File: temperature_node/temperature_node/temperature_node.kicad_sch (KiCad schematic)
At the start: 35 parts, among them CN1 UART, J1 USB_C_Receptacle_USB2.0_16P, J2 S2B-PH-K-S, U1 SHT40-AD1B-R3, U2 MCP73831-2-OT, U3 MIC5504-3.3YM5, U4 ESP32-C3-WROOM-02, U6 USBLC6-2P6

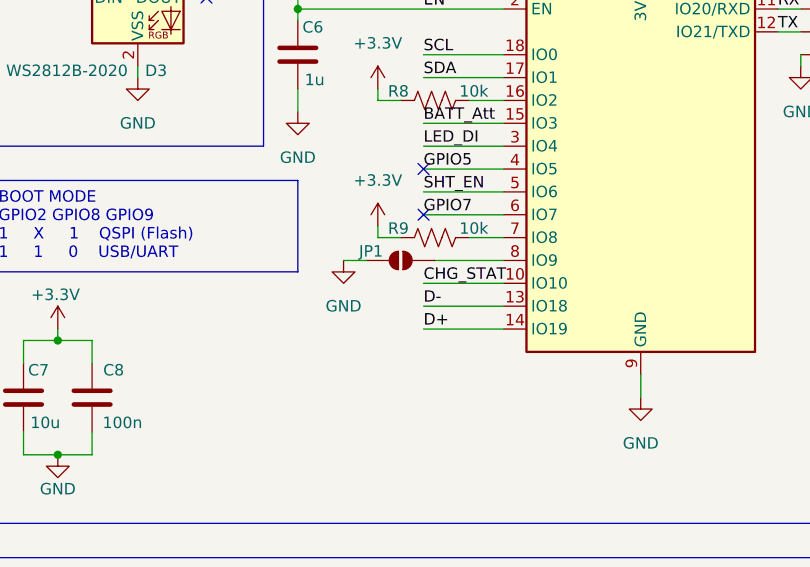
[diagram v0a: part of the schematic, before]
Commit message: Replace pad with side connector for programming enable
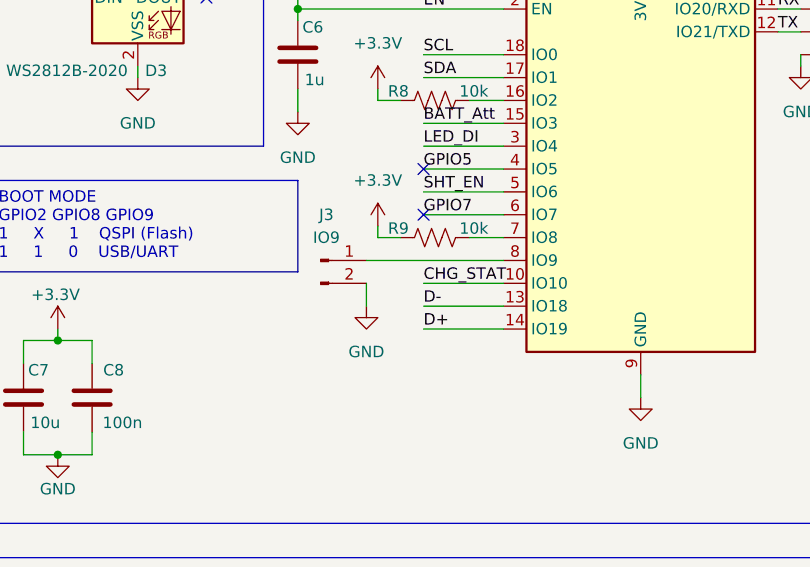
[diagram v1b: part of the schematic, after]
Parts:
- removed JP1: ~, Jumper:SolderJumper-2_P1.3mm_Open_RoundedPad1.0x1.5mm, symbol Jumper:SolderJumper_2_Open
- added J3: IO9, Connector_Wire:SolderWire-0.1sqmm_1x02_P3.6mm_D0.4mm_OD1mm, symbol Connector:Conn_01x02_Pin
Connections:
- net GND: now also J3.2 (Pin_2)
- net at U4.8 (IO9): now also J3.1 (Pin_1)
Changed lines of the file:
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@@
 	(wire
 		(pts
-			(xy 199.39 78.74) (xy 196.85 78.74)
-		)
-		(stroke
-			(width 0)
-			(type default)
-		)
-	)
-	(wire
-		(pts
 			(xy 63.5 52.07) (xy 77.47 52.07)
 		)
@@
 	(wire
 		(pts
+			(xy 199.39 78.74) (xy 214.63 78.74)
+		)
+		(stroke
+			(width 0)
+			(type default)
+		)
+	)
+	(wire
+		(pts
 			(xy 229.87 93.98) (xy 229.87 91.44)
 		)
@@
 	(wire
 		(pts
-			(xy 205.74 63.5) (xy 214.63 63.5)
+			(xy 199.39 81.28) (xy 199.39 83.82)
 		)
 		(stroke
@@
 	(wire
 		(pts
-			(xy 143.51 142.24) (xy 143.51 144.78)
+			(xy 205.74 63.5) (xy 214.63 63.5)
 		)
 		(stroke
@@
 	(wire
 		(pts
-			(xy 208.28 132.08) (xy 208.28 133.35)
+			(xy 143.51 142.24) (xy 143.51 144.78)
 		)
 		(stroke
@@
 	(wire
 		(pts
-			(xy 60.96 74.93) (xy 60.96 73.66)
+			(xy 208.28 132.08) (xy 208.28 133.35)
 		)
 		(stroke
@@
 	(wire
 		(pts
-			(xy 210.82 76.2) (xy 214.63 76.2)
+			(xy 60.96 74.93) (xy 60.96 73.66)
 		)
 		(stroke
@@
 	(wire
 		(pts
-			(xy 99.06 127) (xy 99.06 129.54)
+			(xy 210.82 76.2) (xy 214.63 76.2)
 		)
 		(stroke
@@
 	(wire
 		(pts
-			(xy 205.74 68.58) (xy 214.63 68.58)
+			(xy 99.06 127) (xy 99.06 129.54)
 		)
 		(stroke
@@
 	(wire
 		(pts
-			(xy 207.01 78.74) (xy 214.63 78.74)
+			(xy 205.74 68.58) (xy 214.63 68.58)
 		)
 		(stroke
@@
 	)
 	(symbol
+		(lib_id "Connector:Conn_01x02_Pin")
+		(at 194.31 78.74 0)
+		(unit 1)
+		(exclude_from_sim no)
+		(in_bom yes)
+		(on_board yes)
+		(dnp no)
+		(fields_autoplaced yes)
+		(property "Reference" "J3"
+			(at 194.945 73.66 0)
+			(effects
+				(font
+					(size 1.27 1.27)
+				)
+			)
+		)
+		(property "Value" "IO9"
+			(at 194.945 76.2 0)
+			(effects
+				(font
+					(size 1.27 1.27)
+				)
+			)
+		)
+		(property "Footprint" "Connector_Wire:SolderWire-0.1sqmm_1x02_P3.6mm_D0.4mm_OD1mm"
+			(at 194.31 78.74 0)
+			(effects
+				(font
+					(size 1.27 1.27)
+				)
+				(hide yes)
+			)
+		)
+		(property "Datasheet" "~"
+			(at 194.31 78.74 0)
+			(effects
+				(font
+					(size 1.27 1.27)
+				)
+				(hide yes)
+			)
+		)
+		(property "Description" "Generic connector, single row, 01x02, script generated"
+			(at 194.31 78.74 0)
+			(effects
+				(font
+					(size 1.27 1.27)
+				)
+				(hide yes)
+			)
+		)
+		(pin "1"
+		)
+		(pin "2"
+		)
+		(instances
+			(project ""
+				(path "/b4f604dd-c1be-4776-9f83-5b1c508883b1"
+					(reference "J3")
+					(unit 1)
+				)
+			)
+		)
+	)
+	(symbol
 		(lib_id "Connector:TestPoint")
 		(at 68.58 148.59 0)
@@
 	(symbol
 		(lib_id "power:GND")
-		(at 196.85 78.74 0)
+		(at 199.39 83.82 0)
 		(unit 1)
 		(exclude_from_sim no)
@@
 		(fields_autoplaced yes)
 		(property "Reference" "#PWR014"
-			(at 196.85 85.09 0)
+			(at 199.39 90.17 0)
 			(effects
 				(font
@@
 		)
 		(property "Value" "GND"
-			(at 196.85 83.82 0)
+			(at 199.39 88.9 0)
 			(effects
 				(font
@@
 		)
 		(property "Footprint" ""
-			(at 196.85 78.74 0)
+			(at 199.39 83.82 0)
 			(effects
 				(font
@@
 		)
 		(property "Datasheet" ""
-			(at 196.85 78.74 0)
+			(at 199.39 83.82 0)
 			(effects
 				(font
@@
 		)
 		(property "Description" "Power symbol creates a global label with name \"GND\" , ground"
-			(at 196.85 78.74 0)
+			(at 199.39 83.82 0)
 			(effects
 				(font
@@
 					(unit 1)
 				)
-			)
-		)
-	)
-	(symbol
-		(lib_id "Jumper:SolderJumper_2_Open")
-		(at 203.2 78.74 0)
-		(unit 1)
-		(exclude_from_sim yes)
-		(in_bom no)
-		(on_board yes)
-		(dnp no)
-		(property "Reference" "JP1"
-			(at 199.898 77.724 0)
-			(effects
-				(font
-					(size 1.27 1.27)
-				)
-			)
-		)
-		(property "Value" "~"
-			(at 203.2 74.93 0)
-			(effects
-				(font
-					(size 1.27 1.27)
-				)
-			)
-		)
-		(property "Footprint" "Jumper:SolderJumper-2_P1.3mm_Open_RoundedPad1.0x1.5mm"
-			(at 203.2 78.74 0)
-			(effects
-				(font
-					(size 1.27 1.27)
-				)
-				(hide yes)
-			)
-		)
-		(property "Datasheet" "~"
-			(at 203.2 78.74 0)
-			(effects
-				(font
-					(size 1.27 1.27)
-				)
-				(hide yes)
-			)
-		)
-		(property "Description" "Solder Jumper, 2-pole, open"
-			(at 203.2 78.74 0)
-			(effects
-				(font
-					(size 1.27 1.27)
-				)
-				(hide yes)
-			)
-		)
-		(pin "2"
-		)
-		(pin "1"
-		)
-		(instances
-			(project ""
-				(path "/b4f604dd-c1be-4776-9f83-5b1c508883b1"
-					(reference "JP1")
-					(unit 1)
-				)

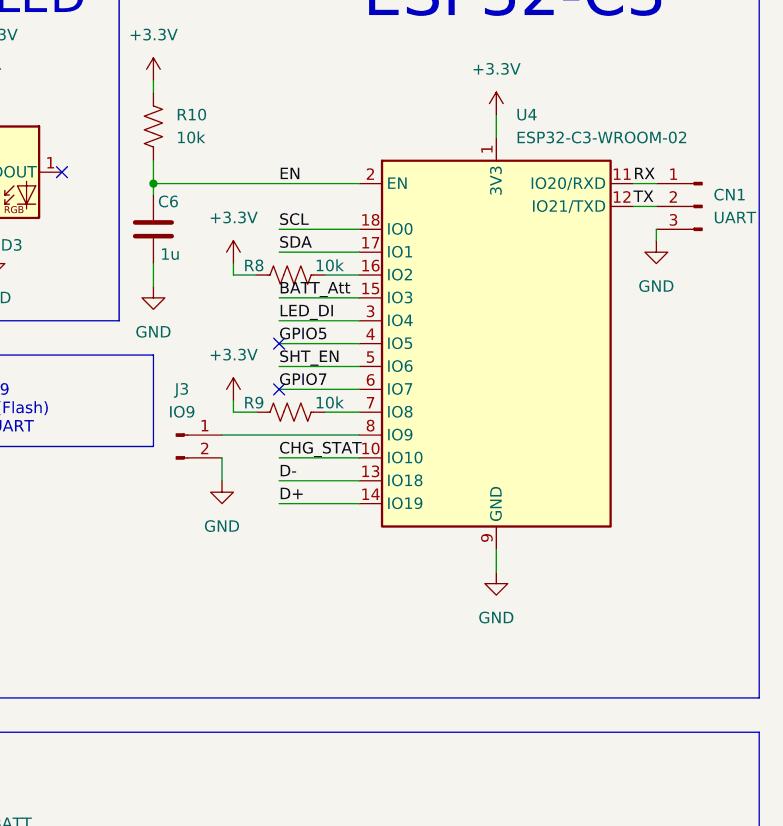
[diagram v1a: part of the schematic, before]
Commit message: Replace header connector with testpoint
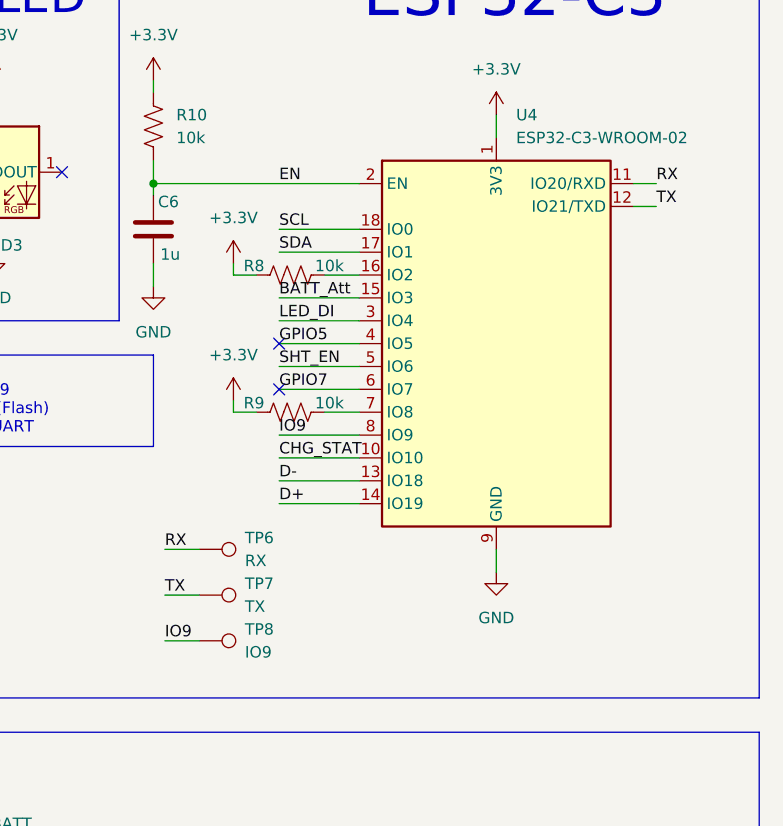
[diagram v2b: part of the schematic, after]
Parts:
- removed CN1: UART, Connector_Wire:SolderWire-0.1sqmm_1x03_P3.6mm_D0.4mm_OD1mm, symbol Connector:Conn_01x03_Pin
- removed J3: IO9, Connector_Wire:SolderWire-0.1sqmm_1x02_P3.6mm_D0.4mm_OD1mm, symbol Connector:Conn_01x02_Pin
- added TP6: RX, TestPoint:TestPoint_Pad_D1.0mm, symbol Connector:TestPoint
- added TP7: TX, TestPoint:TestPoint_Pad_D1.0mm, symbol Connector:TestPoint
- added TP8: IO9, TestPoint:TestPoint_Pad_D1.0mm, symbol Connector:TestPoint
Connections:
- net RX: now also TP6.1
- net TX: now also TP7.1
- net IO9: now reaches U4.8 (IO9)
- net IO9: now also TP8.1

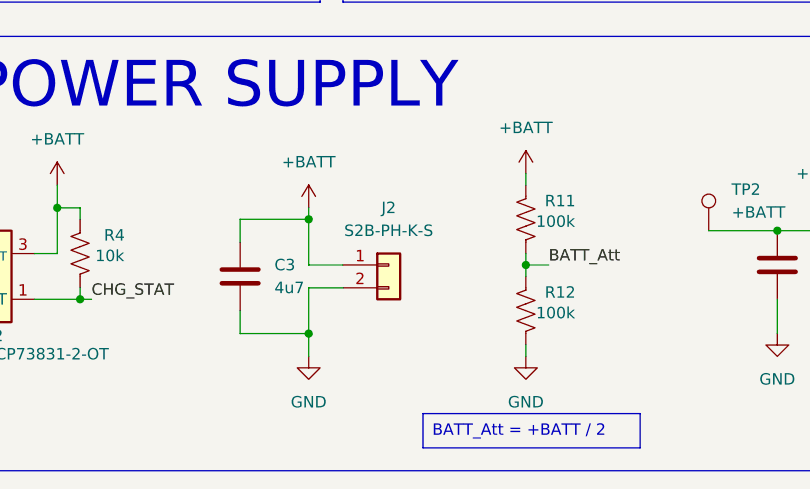
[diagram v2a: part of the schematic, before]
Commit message: Add note for battery and fix wrong reference for battery connector
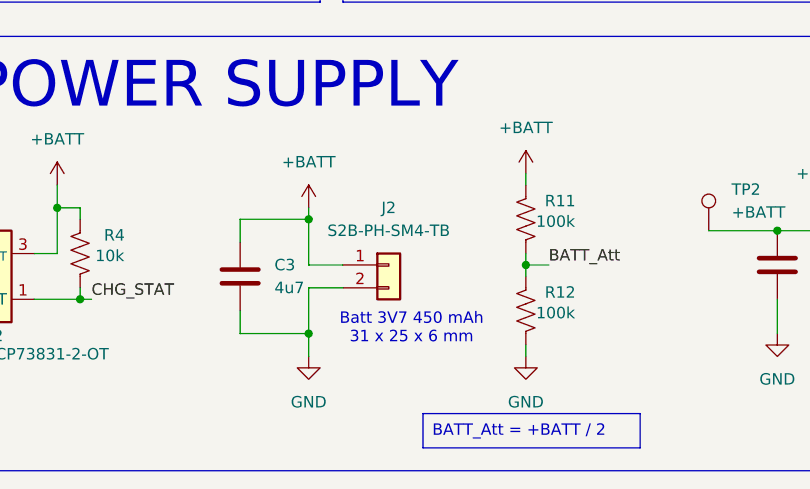
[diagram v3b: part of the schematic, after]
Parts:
- J2: value S2B-PH-K-S -> S2B-PH-SM4-TB
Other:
- note added: "Batt 3V7 450 mAh 31 x 25 x 6 mm"
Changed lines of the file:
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@@
+		)
+	)
+	(text "Batt 3V7 450 mAh\n31 x 25 x 6 mm"
+		(exclude_from_sim no)
+		(at 162.56 144.272 0)
+		(effects
+			(font
+				(size 1.27 1.27)
+			)
+			(href "https://powercells.de/lipo-450mah-3-7v-akku-battery-3-6v-akku-jst-ph-2-0-lithium-ion-polymer-426.html")
 		)
 	)
@@
 			)
 		)
-		(property "Value" "S2B-PH-K-S"
+		(property "Value" "S2B-PH-SM4-TB"
 			(at 160.02 133.35 0)
 			(effects

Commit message: Reanotate PCB and SCH
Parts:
- J2: value S2B-PH-SM4-TB -> S2B-PH-K-S
- renumbered C6 to C2, C8 to C3, C7 to C4, C3 to C6, C4 to C7, C9 to C8, C2 to C9, D3 to D1, R2 to R1, R4 to R10, R9 to R11, R10 to R2, R8 to R3, R1 to R4, R3 to R5, R5 to R6, R11 to R7, R12 to R8, R6 to R9, TP6 to TP1, TP4 to TP2, TP7 to TP4, TP1 to TP6, TP8 to TP7, TP2 to TP8, U4 to U1, U1 to U2, U2 to U3, U6 to U4, U3 to U5
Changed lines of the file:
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@@
 		(on_board yes)
 		(dnp no)
-		(property "Reference" "R9"
+		(property "Reference" "R11"
 			(at 202.946 75.184 90)
 			(effects
@@
 			(project "temperature_node"
 				(path "/b4f604dd-c1be-4776-9f83-5b1c508883b1"
-					(reference "R9")
+					(reference "R11")
 					(unit 1)
 				)
@@
 		(dnp no)
 		(fields_autoplaced yes)
-		(property "Reference" "TP1"
+		(property "Reference" "TP6"
 			(at 107.95 123.6979 0)
 			(effects
@@
 			(project "temperature_node"
 				(path "/b4f604dd-c1be-4776-9f83-5b1c508883b1"
-					(reference "TP1")
+					(reference "TP6")
 					(unit 1)
 				)
@@
 		(on_board yes)
 		(dnp no)
-		(property "Reference" "U2"
+		(property "Reference" "U3"
 			(at 114.808 145.034 0)
 			(effects
@@
 			(project ""
 				(path "/b4f604dd-c1be-4776-9f83-5b1c508883b1"
-					(reference "U2")
+					(reference "U3")
 					(unit 1)
 				)
@@
 			)
 		)
-		(property "Value" "S2B-PH-SM4-TB"
+		(property "Value" "S2B-PH-K-S"
 			(at 160.02 133.35 0)
 			(effects
@@
 		(dnp no)
 		(fields_autoplaced yes)
-		(property "Reference" "TP6"
+		(property "Reference" "TP1"
 			(at 201.93 90.1699 90)
 			(effects
@@
 			(project ""
 				(path "/b4f604dd-c1be-4776-9f83-5b1c508883b1"
-					(reference "TP6")
+					(reference "TP1")
 					(unit 1)
 				)
@@
 		(dnp no)
 		(fields_autoplaced yes)
-		(property "Reference" "TP7"
+		(property "Reference" "TP4"
 			(at 201.93 95.2499 90)
 			(effects
@@
 			(project "temperature_node"
 				(path "/b4f604dd-c1be-4776-9f83-5b1c508883b1"
-					(reference "TP7")
+					(reference "TP4")
 					(unit 1)
 				)
@@
 		(dnp no)
 		(fields_autoplaced yes)
-		(property "Reference" "TP8"
+		(property "Reference" "TP7"
 			(at 201.93 100.3299 90)
 			(effects
@@
 			(project "temperature_node"
 				(path "/b4f604dd-c1be-4776-9f83-5b1c508883b1"
-					(reference "TP8")
+					(reference "TP7")
 					(unit 1)
 				)
@@
 		(on_board yes)
 		(dnp no)
-		(property "Reference" "D3"
+		(property "Reference" "D1"
 			(at 176.022 57.658 0)
 			(effects
@@
 			(project ""
 				(path "/b4f604dd-c1be-4776-9f83-5b1c508883b1"
-					(reference "D3")
+					(reference "D1")
 					(unit 1)
 				)
@@
 		(on_board yes)
 		(dnp no)
-		(property "Reference" "C8"
+		(property "Reference" "C3"
 			(at 172.466 90.932 0)
 			(effects
@@
 			(project "temperature_node"
 				(path "/b4f604dd-c1be-4776-9f83-5b1c508883b1"
-					(reference "C8")
+					(reference "C3")
 					(unit 1)
 				)
@@
 		(dnp no)
 		(fields_autoplaced yes)
-		(property "Reference" "U4"
+		(property "Reference" "U1"
 			(at 232.0641 43.18 0)
 			(effects
@@
 			(project ""
 				(path "/b4f604dd-c1be-4776-9f83-5b1c508883b1"
-					(reference "U4")
+					(reference "U1")
 					(unit 1)
 				)
@@
 		(dnp no)
 		(fields_autoplaced yes)
-		(property "Reference" "TP4"
+		(property "Reference" "TP2"
 			(at 53.34 51.3079 0)
 			(effects
@@
 			(project "temperature_node"
 				(path "/b4f604dd-c1be-4776-9f83-5b1c508883b1"
-					(reference "TP4")
+					(reference "TP2")
 					(unit 1)
 				)
@@
 		(on_board yes)
 		(dnp no)
-		(property "Reference" "R6"
+		(property "Reference" "R9"
 			(at 125.476 56.134 90)
 			(effects
@@
 			(project "temperature_node"
 				(path "/b4f604dd-c1be-4776-9f83-5b1c508883b1"
-					(reference "R6")
+					(reference "R9")
 					(unit 1)
 				)
@@
 		(on_board yes)
 		(dnp no)
-		(property "Reference" "C7"
+		(property "Reference" "C4"
 			(at 161.798 90.932 0)
 			(effects
@@
 			(project "temperature_node"
 				(path "/b4f604dd-c1be-4776-9f83-5b1c508883b1"
-					(reference "C7")
+					(reference "C4")
 					(unit 1)
 				)
@@
 		(on_board yes)
 		(dnp no)
-		(property "Reference" "R1"
+		(property "Reference" "R4"
 			(at 73.66 56.642 0)
 			(effects
@@
 			(project "temperature_node"
 				(path "/b4f604dd-c1be-4776-9f83-5b1c508883b1"
-					(reference "R1")
+					(reference "R4")
 					(unit 1)
 				)
@@
 		(on_board yes)
 		(dnp no)
-		(property "Reference" "C9"
+		(property "Reference" "C8"
 			(at 149.606 79.502 0)
 			(effects
@@
 			(project "temperature_node"
 				(path "/b4f604dd-c1be-4776-9f83-5b1c508883b1"
-					(reference "C9")
+					(reference "C8")
 					(unit 1)
 				)
@@
 		(on_board yes)
 		(dnp no)
-		(property "Reference" "C3"
+		(property "Reference" "C6"
 			(at 147.32 137.1599 0)
 			(effects
@@
 			(project "temperature_node"
 				(path "/b4f604dd-c1be-4776-9f83-5b1c508883b1"
-					(reference "C3")
+					(reference "C6")
 					(unit 1)
 				)
@@
 		(dnp no)
 		(fields_autoplaced yes)
-		(property "Reference" "C4"
+		(property "Reference" "C7"
 			(at 207.01 135.8899 0)
 			(effects
@@
 			(project "temperature_node"
 				(path "/b4f604dd-c1be-4776-9f83-5b1c508883b1"
-					(reference "C4")
+					(reference "C7")
 					(unit 1)
 				)
@@
 		(on_board yes)
 		(dnp no)
-		(property "Reference" "U1"
+		(property "Reference" "U2"
 			(at 65.024 71.374 0)
 			(effects
@@
 			(project ""
 				(path "/b4f604dd-c1be-4776-9f83-5b1c508883b1"
-					(reference "U1")
+					(reference "U2")
 					(unit 1)
 				)
@@
 		(on_board yes)
 		(dnp no)
-		(property "Reference" "R2"
+		(property "Reference" "R1"
 			(at 83.82 61.468 0)
 			(effects
@@
 			(project "temperature_node"
 				(path "/b4f604dd-c1be-4776-9f83-5b1c508883b1"
-					(reference "R2")
+					(reference "R1")
 					(unit 1)
 				)
@@
 		(on_board yes)
 		(dnp no)
-		(property "Reference" "C6"
+		(property "Reference" "C2"
 			(at 192.278 52.832 0)
 			(effects
@@
 			(project ""
 				(path "/b4f604dd-c1be-4776-9f83-5b1c508883b1"
-					(reference "C6")
+					(reference "C2")
 					(unit 1)
 				)
@@
 		(dnp no)
 		(fields_autoplaced yes)
-		(property "Reference" "U3"
+		(property "Reference" "U5"
 			(at 222.25 125.73 0)
 			(effects
@@
 			(project ""
 				(path "/b4f604dd-c1be-4776-9f83-5b1c508883b1"
-					(reference "U3")
+					(reference "U5")
 					(unit 1)
 				)
@@
 		(dnp no)
 		(fields_autoplaced yes)
-		(property "Reference" "R10"
+		(property "Reference" "R2"
 			(at 194.31 43.1799 0)
 			(effects
@@
 			(project ""
 				(path "/b4f604dd-c1be-4776-9f83-5b1c508883b1"
-					(reference "R10")
+					(reference "R2")
 					(unit 1)
 				)
@@
 		(on_board yes)
 		(dnp no)
-		(property "Reference" "R12"
+		(property "Reference" "R8"
 			(at 179.07 140.208 0)
 			(effects
@@
 			(project "temperature_node"
 				(path "/b4f604dd-c1be-4776-9f83-5b1c508883b1"
-					(reference "R12")
+					(reference "R8")
 					(unit 1)
 				)
@@
 		(on_board yes)
 		(dnp no)
-		(property "Reference" "R3"
+		(property "Reference" "R5"
 			(at 102.87 145.288 0)
 			(effects
@@
 			(project "temperature_node"
 				(path "/b4f604dd-c1be-4776-9f83-5b1c508883b1"
-					(reference "R3")
+					(reference "R5")
 					(unit 1)
 				)
@@
 		(dnp no)
 		(fields_autoplaced yes)
-		(property "Reference" "C2"
+		(property "Reference" "C9"
 			(at 97.79 134.6199 0)
 			(effects
@@
 			(project ""
 				(path "/b4f604dd-c1be-4776-9f83-5b1c508883b1"
-					(reference "C2")
+					(reference "C9")
 					(unit 1)
 				)
@@
 		(dnp no)
 		(fields_autoplaced yes)
-		(property "Reference" "U6"
+		(property "Reference" "U4"
 			(at 136.2711 64.77 0)
 			(effects
@@
 			(project ""
 				(path "/b4f604dd-c1be-4776-9f83-5b1c508883b1"
-					(reference "U6")
+					(reference "U4")
 					(unit 1)
 				)
@@
 		(on_board yes)
 		(dnp no)
-		(property "Reference" "R11"
+		(property "Reference" "R7"
 			(at 179.07 130.048 0)
 			(effects
@@
 			(project "temperature_node"
 				(path "/b4f604dd-c1be-4776-9f83-5b1c508883b1"
-					(reference "R11")
+					(reference "R7")
 					(unit 1)
 				)
@@
 		(dnp no)
 		(fields_autoplaced yes)
-		(property "Reference" "TP2"
+		(property "Reference" "TP8"
 			(at 198.12 128.7779 0)
 			(effects
@@
 			(project "temperature_node"
 				(path "/b4f604dd-c1be-4776-9f83-5b1c508883b1"
-					(reference "TP2")
+					(reference "TP8")
 					(unit 1)
 				)
@@
 		(on_board yes)
 		(dnp no)
-		(property "Reference" "R5"
+		(property "Reference" "R6"
 			(at 125.476 53.594 90)
 			(effects
@@
 			(project "temperature_node"
 				(path "/b4f604dd-c1be-4776-9f83-5b1c508883b1"
-					(reference "R5")
+					(reference "R6")
 					(unit 1)
 				)
@@
 		(on_board yes)
 		(dnp no)
-		(property "Reference" "R8"
+		(property "Reference" "R3"
 			(at 202.946 59.944 90)
 			(effects
@@
 			(project "temperature_node"
 				(path "/b4f604dd-c1be-4776-9f83-5b1c508883b1"
-					(reference "R8")
+					(reference "R3")
 					(unit 1)
 				)
@@
 		(on_board yes)
 		(dnp no)
-		(property "Reference" "R4"
+		(property "Reference" "R10"
 			(at 129.54 133.858 0)
 			(effects
@@
 			(project "temperature_node"
 				(path "/b4f604dd-c1be-4776-9f83-5b1c508883b1"
-					(reference "R4")
+					(reference "R10")
 					(unit 1)
 				)
